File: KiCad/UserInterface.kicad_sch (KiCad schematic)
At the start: 36 parts, among them J3 LCD_Conn, J4 Enc_Conn, J5 Btn_Matrix, J6 Btn&Led, J7 PWR, SW1 SW_Push_45deg, SW10 SW_Push_45deg, SW11 SW_Push_45deg, SW12 SW_Push_45deg, SW13 SW_Push_45deg, SW14 SW_Push_45deg, SW15 SW_Push_45deg, SW16 SW_Push_45deg, SW17 SW_Push_45deg, SW18 SW_Push, SW19 SW_Push, SW2 SW_Push_45deg, SW3 SW_Push_45deg, SW4 SW_Push_45deg, SW5 SW_Push_45deg, SW6 SW_Push_45deg, SW7 SW_Push_45deg, SW8 SW_Push_45deg, SW9 RotaryEncoder_Switch

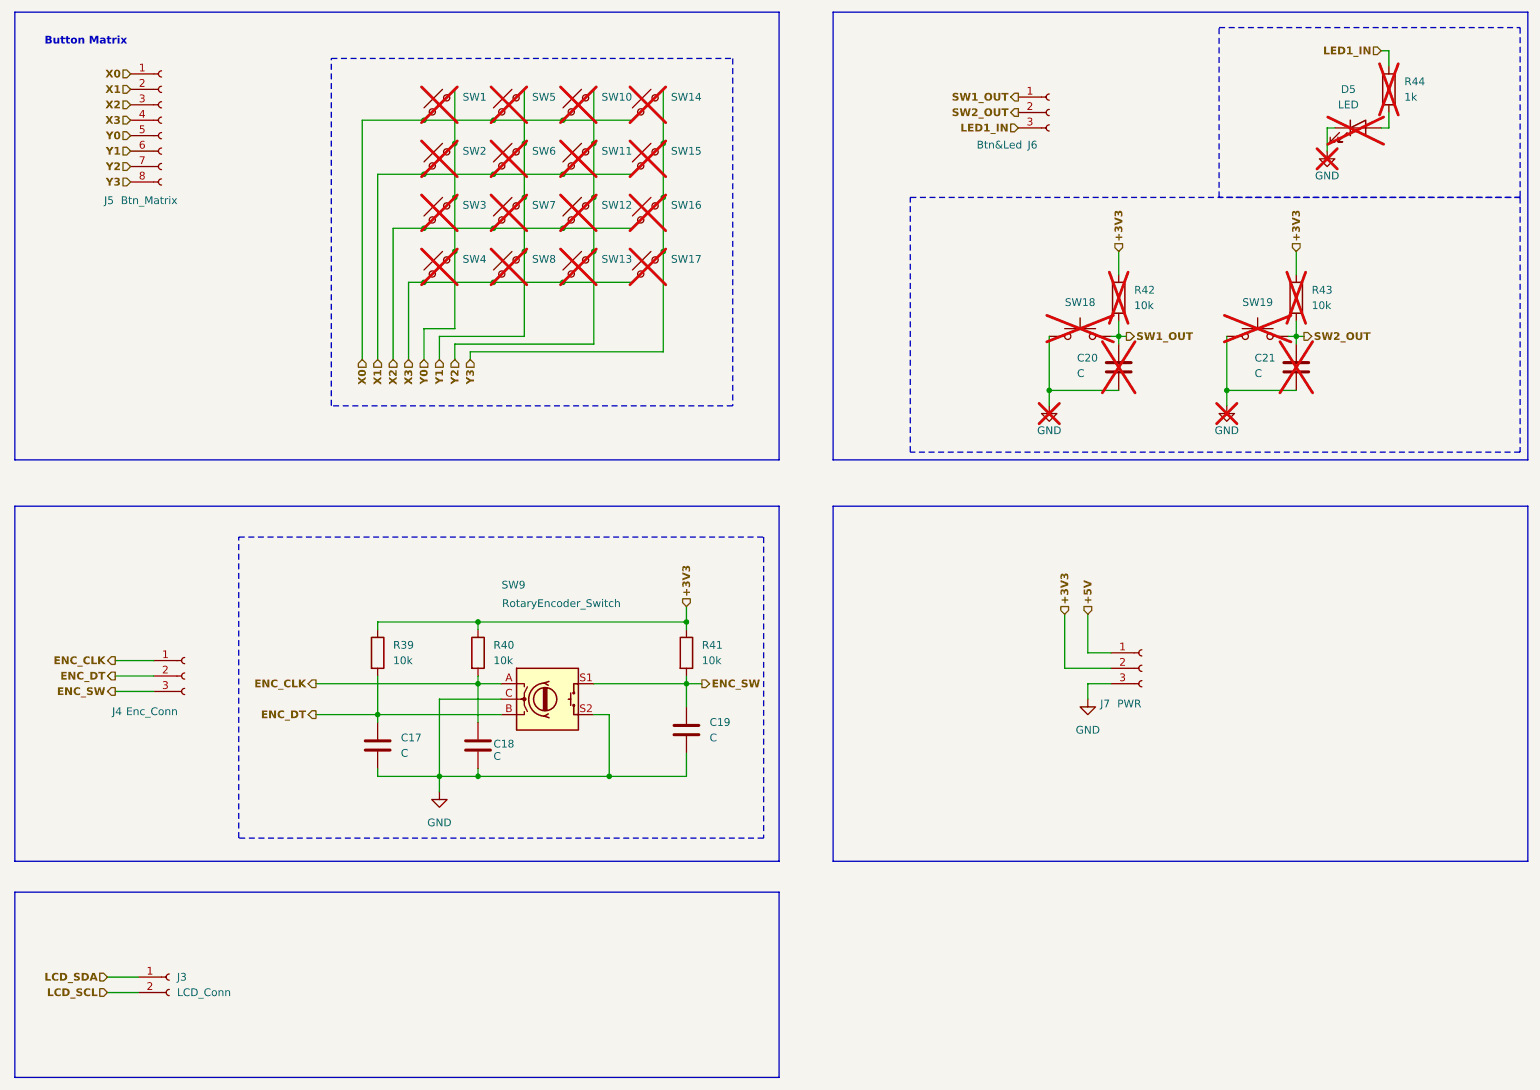
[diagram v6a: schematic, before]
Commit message: Tidied up schematic, changed footprints
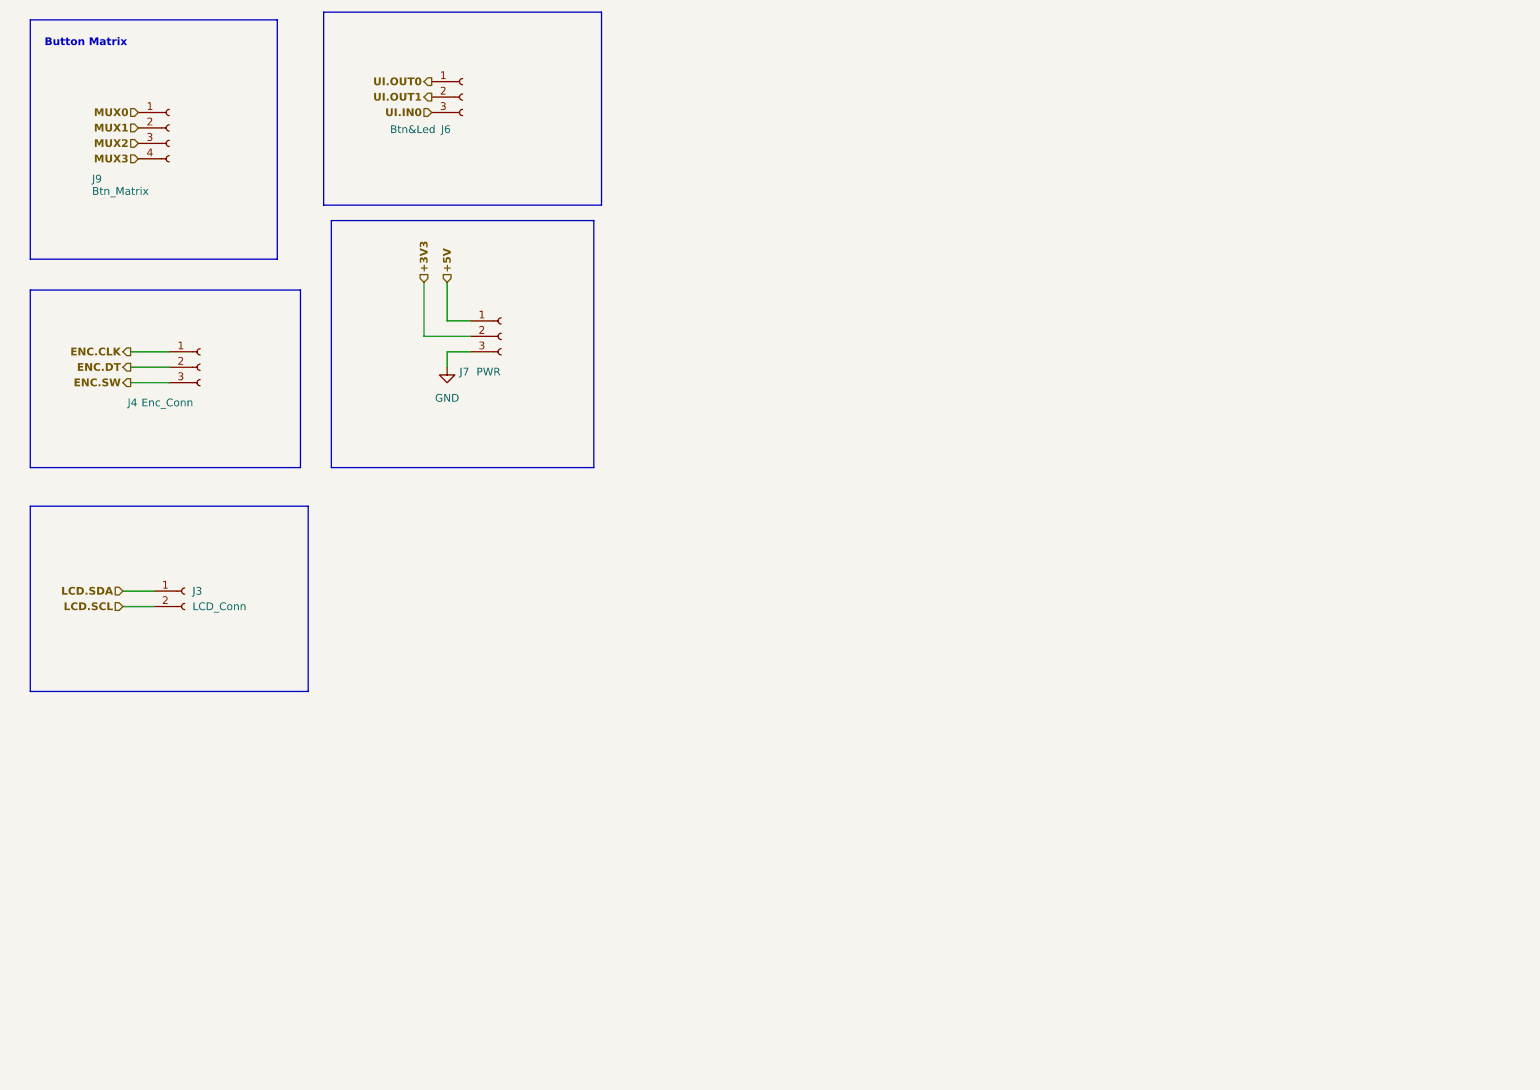
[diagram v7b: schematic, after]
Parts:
- removed C17, C18, C19, C20, C21: C, symbol Device:C
- removed D5: LED, symbol Device:LED
- removed J5: Btn_Matrix, Connector_PinSocket_2.54mm:PinSocket_1x08_P2.54mm_Vertical, symbol Connector:Conn_01x08_Socket
- removed R39, R40, R41, R42, R43: 10k, symbol Device:R
- removed R44: 1k, symbol Device:R
- removed SW1, SW10, SW11, SW12, SW13, SW14, SW15, SW16, SW17, SW2, SW3, SW4, SW5, SW6, SW7, SW8: SW_Push_45deg, symbol Switch:SW_Push_45deg
- removed SW18, SW19: SW_Push, symbol Switch:SW_Push
- removed SW9: RotaryEncoder_Switch, symbol Device:RotaryEncoder_Switch
- added J9: Btn_Matrix, Connector_PinSocket_2.54mm:PinSocket_1x04_P2.54mm_Vertical, symbol Connector:Conn_01x04_Socket
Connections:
- net ENC_CLK renamed ENC.CLK
- net ENC_DT renamed ENC.DT
- net ENC_SW renamed ENC.SW
- net LCD_SCL renamed LCD.SCL
- net LCD_SDA renamed LCD.SDA
- net LED1_IN renamed UI.IN0
- net SW1_OUT renamed UI.OUT0
- net SW2_OUT renamed UI.OUT1
- new net MUX0: J9.1 (Pin_1)
- new net MUX1: J9.2 (Pin_2)
- new net MUX2: J9.3 (Pin_3)
- new net MUX3: J9.4 (Pin_4)
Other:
- moved on the sheet: J3, J4, J6, J7

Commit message: Alfa version of PCB design
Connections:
- net +3V3: now also J7.1 (Pin_1); no longer J7.2 (Pin_2)
- net +5V: now also J7.2 (Pin_2); no longer J7.1 (Pin_1)
- net ENC.CLK: now also J4.2 (Pin_2); no longer J4.1 (Pin_1)
- net ENC.DT: now also J4.1 (Pin_1); no longer J4.2 (Pin_2)
- net MUX2: now also J9.4 (Pin_4); no longer J9.3 (Pin_3)
- net MUX3: now also J9.3 (Pin_3); no longer J9.4 (Pin_4)
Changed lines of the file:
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@@
 	(hierarchical_label "ENC.CLK"
 		(shape output)
-		(at 39.37 73.66 180)
+		(at 39.37 76.2 180)
 		(fields_autoplaced yes)
 		(effects
@@
 	(hierarchical_label "MUX2"
 		(shape input)
-		(at 40.64 39.37 180)
+		(at 40.64 41.91 180)
 		(fields_autoplaced yes)
 		(effects
@@
 	(hierarchical_label "+5V"
 		(shape input)
-		(at 91.44 62.23 90)
+		(at 87.63 62.23 90)
 		(fields_autoplaced yes)
 		(effects
@@
 	(hierarchical_label "ENC.DT"
 		(shape output)
-		(at 39.37 76.2 180)
+		(at 39.37 73.66 180)
 		(fields_autoplaced yes)
 		(effects
@@
 	(hierarchical_label "+3V3"
 		(shape input)
-		(at 87.63 62.23 90)
+		(at 91.44 62.23 90)
 		(fields_autoplaced yes)
 		(effects
@@
 	(hierarchical_label "MUX3"
 		(shape input)
-		(at 40.64 41.91 180)
+		(at 40.64 39.37 180)
 		(fields_autoplaced yes)
 		(effects
